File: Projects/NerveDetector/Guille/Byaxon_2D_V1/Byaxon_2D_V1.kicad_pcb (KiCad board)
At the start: 2 copper layers, 102 x 49 mm, 74 parts, among them U1 TL074

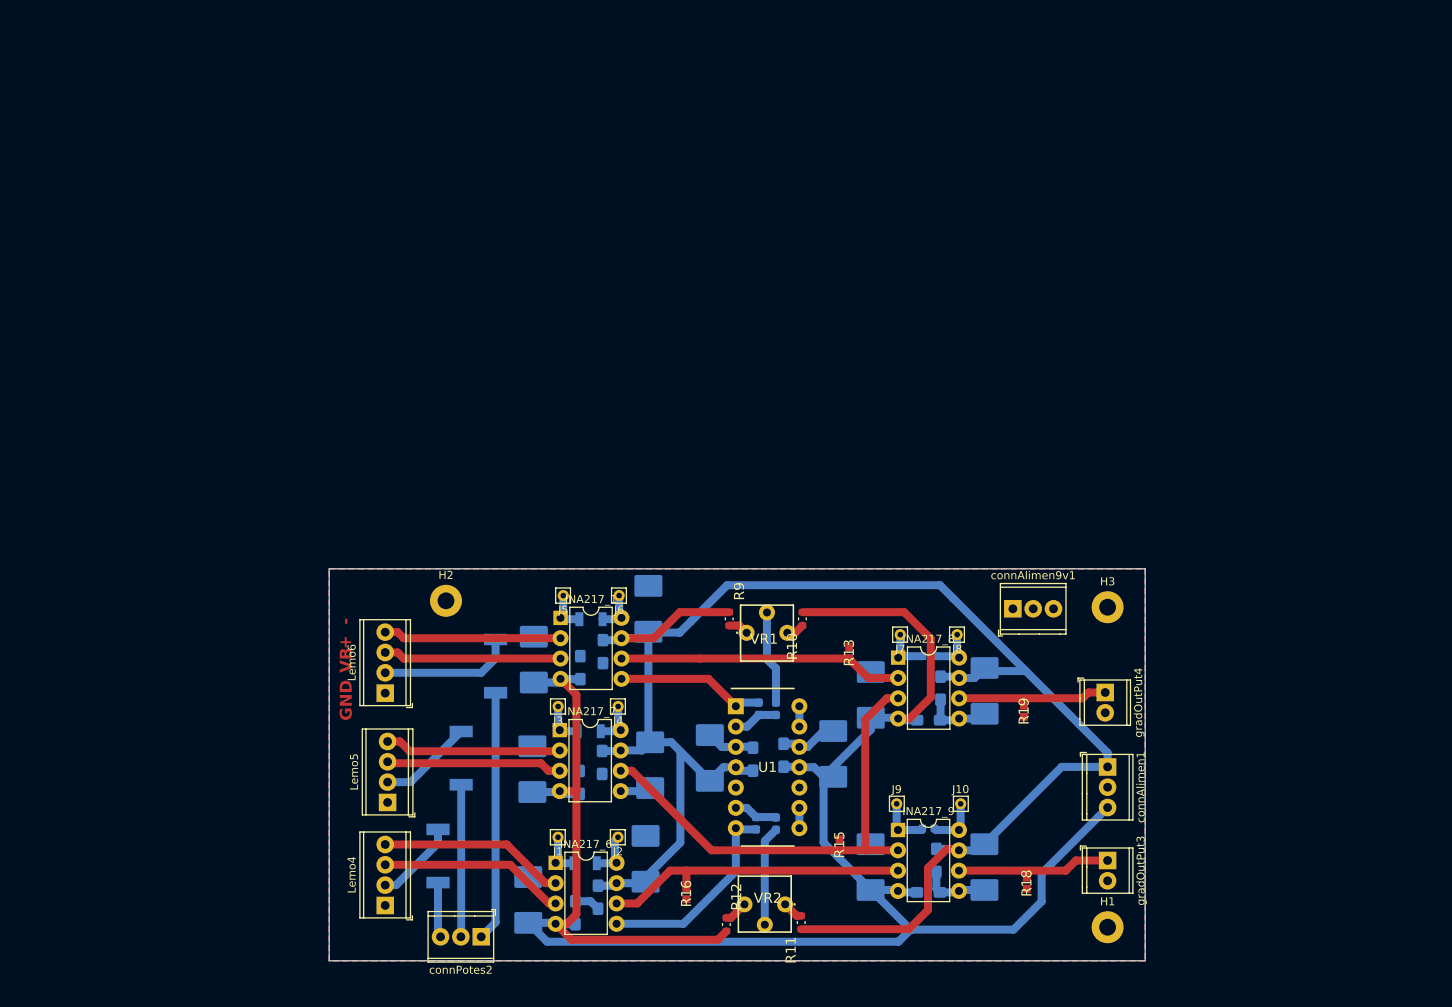
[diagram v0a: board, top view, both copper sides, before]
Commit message: Solved problem with footprint libraries missing
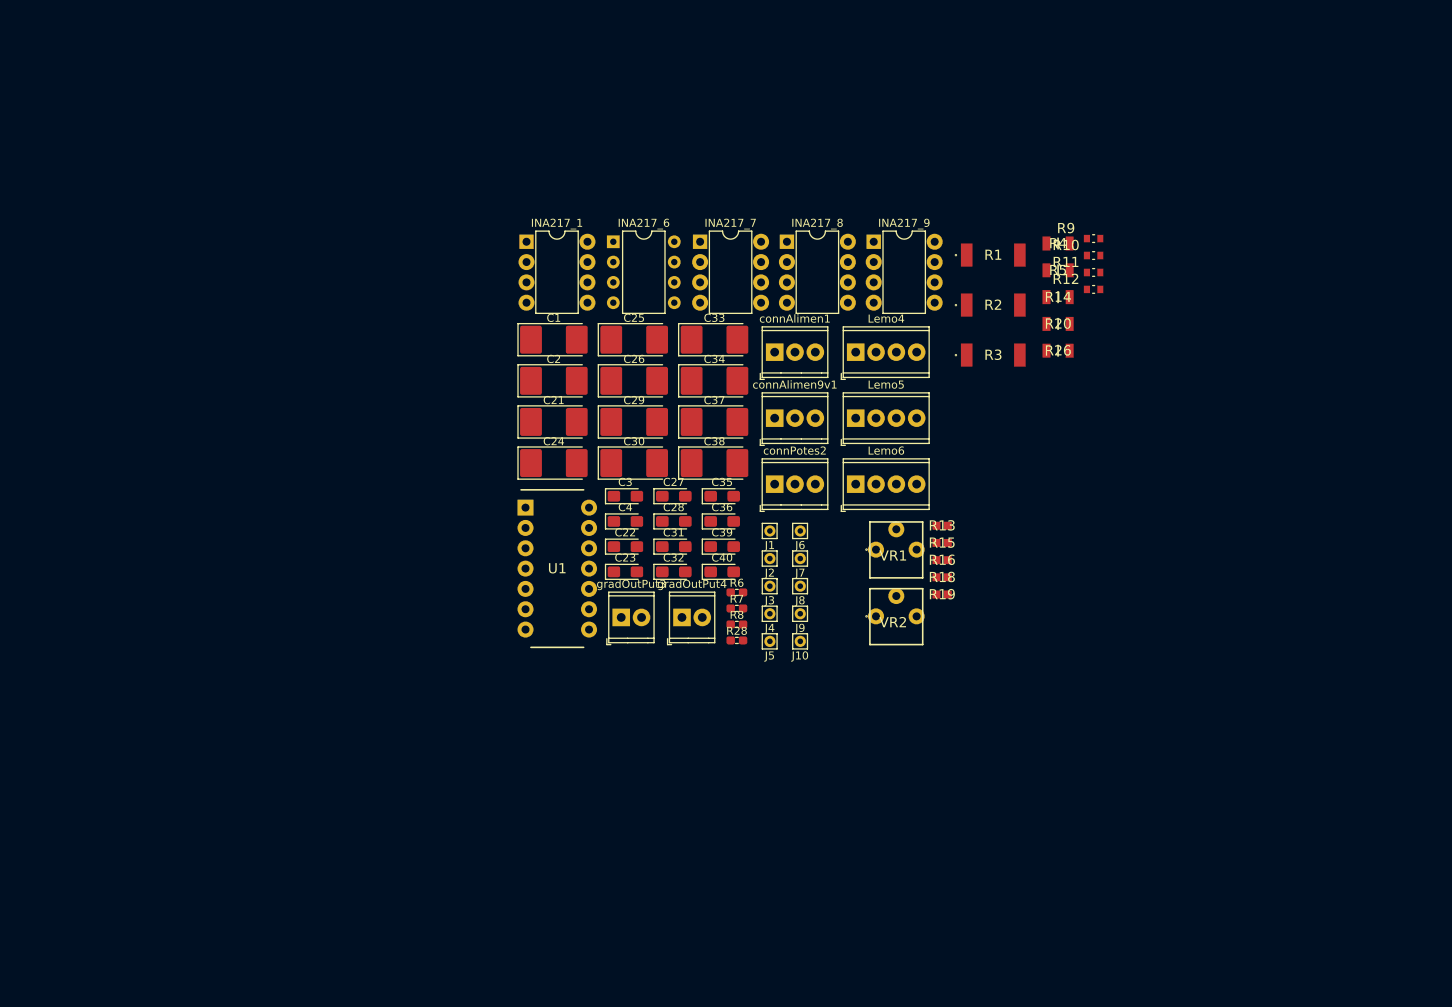
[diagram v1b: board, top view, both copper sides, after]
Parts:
- removed H1, H2, H3: MountingHole_Pad, Library_Acid_etch_limitations:MountingHole_2.1mm_Acid_Etch_Limitations
- C1, C2, C21, C22, C23, C24, C25, C26, C27, C28, C29, C3, C30, C31, C32, C33, C34, C35, C36, C37, C38, C39, C4, C40, R28, R6, R7, R8: moved to F.Cu
- R1, R2, R3: footprint SamacSys_Parts:ERJ1T__2512_ -> Samac_sys:ERJ1T__2512_; moved to F.Cu
- R10, R11, R12, R9: footprint SamacSys_Parts:RESC1608X60N -> Samac_sys:RESC1608X60N
- R14, R20: footprint SamacSys_Parts:RESC1608X55N -> Samac_sys:RESC3016X65N; moved to F.Cu
- R26, R4, R5: footprint SamacSys_Parts:RESC3016X65N -> Samac_sys:RESC3016X65N; moved to F.Cu
- moved R2 97.8 mm to (153.0, 73.0), turned to 0 degrees
- moved R5 94.8 mm to (161.1, 68.7)
- moved R12 91.7 mm to (165.6, 71.1), turned to 0 degrees
- moved R1 91.5 mm to (153.0, 66.8), turned to 0 degrees
- moved Lemo4 90.8 mm to (135.8, 78.9), turned to 0 degrees
- moved R11 89.1 mm to (165.6, 69.0), turned to 0 degrees
- moved R4 84.6 mm to (161.1, 65.3)
- moved C25 79.1 mm to (108.1, 77.4), turned to 0 degrees
- moved INA217_6 78.0 mm to (105.5, 65.1)
- moved Lemo5 75.7 mm to (135.8, 87.2), turned to 0 degrees
- moved INA217_9 73.6 mm to (138.1, 65.1)
- moved R3 73.4 mm to (153.0, 79.3), turned to 0 degrees
- moved R14 68.4 mm to (161.1, 72.0)
- moved gradOutPut3 68.0 mm to (106.5, 112.1), turned to 0 degrees
- moved connPotes2 67.4 mm to (125.7, 95.4), turned to 0 degrees
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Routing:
- net -13: track 239.3 -> 0.00 mm
- net +13: track 215.2 -> 0.00 mm
- net Net-(INA217_8-+): track 60.6 -> 0.00 mm
- net Net-(INA217_9-+): track 38.9 -> 0.00 mm
- net Earth: track 36.4 -> 0.00 mm
- net Net-(INA217_8--): track 35.6 -> 0.00 mm
- net Net-(connPotes2-Pin_1): track 31.3 -> 0.00 mm
- net Net-(INA217_6-Ref): track 25.6 -> 0.00 mm
- net Net-(INA217_6-+): track 23.3 -> 0.00 mm
- net Net-(INA217_6--): track 23.3 -> 0.00 mm
- net Net-(INA217_1-+): track 22.2 -> 0.00 mm
- net Net-(INA217_1--): track 22.2 -> 0.00 mm
- net Net-(INA217_7-+): track 22.0 -> 0.00 mm
- net Net-(INA217_7--): track 21.7 -> 0.00 mm
- net Net-(gradOutPut3-Pin_1): track 19.1 -> 0.00 mm
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- removed copper zone on B.Cu, net Earth
- removed copper zone on F.Cu, net Earth
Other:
- board outline removed
- board text removed: "+"
- board text removed: "-"
- board text removed: "GND"
- board text removed: "VB"

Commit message: Layed out bigger edge cut, added jumper to Voss
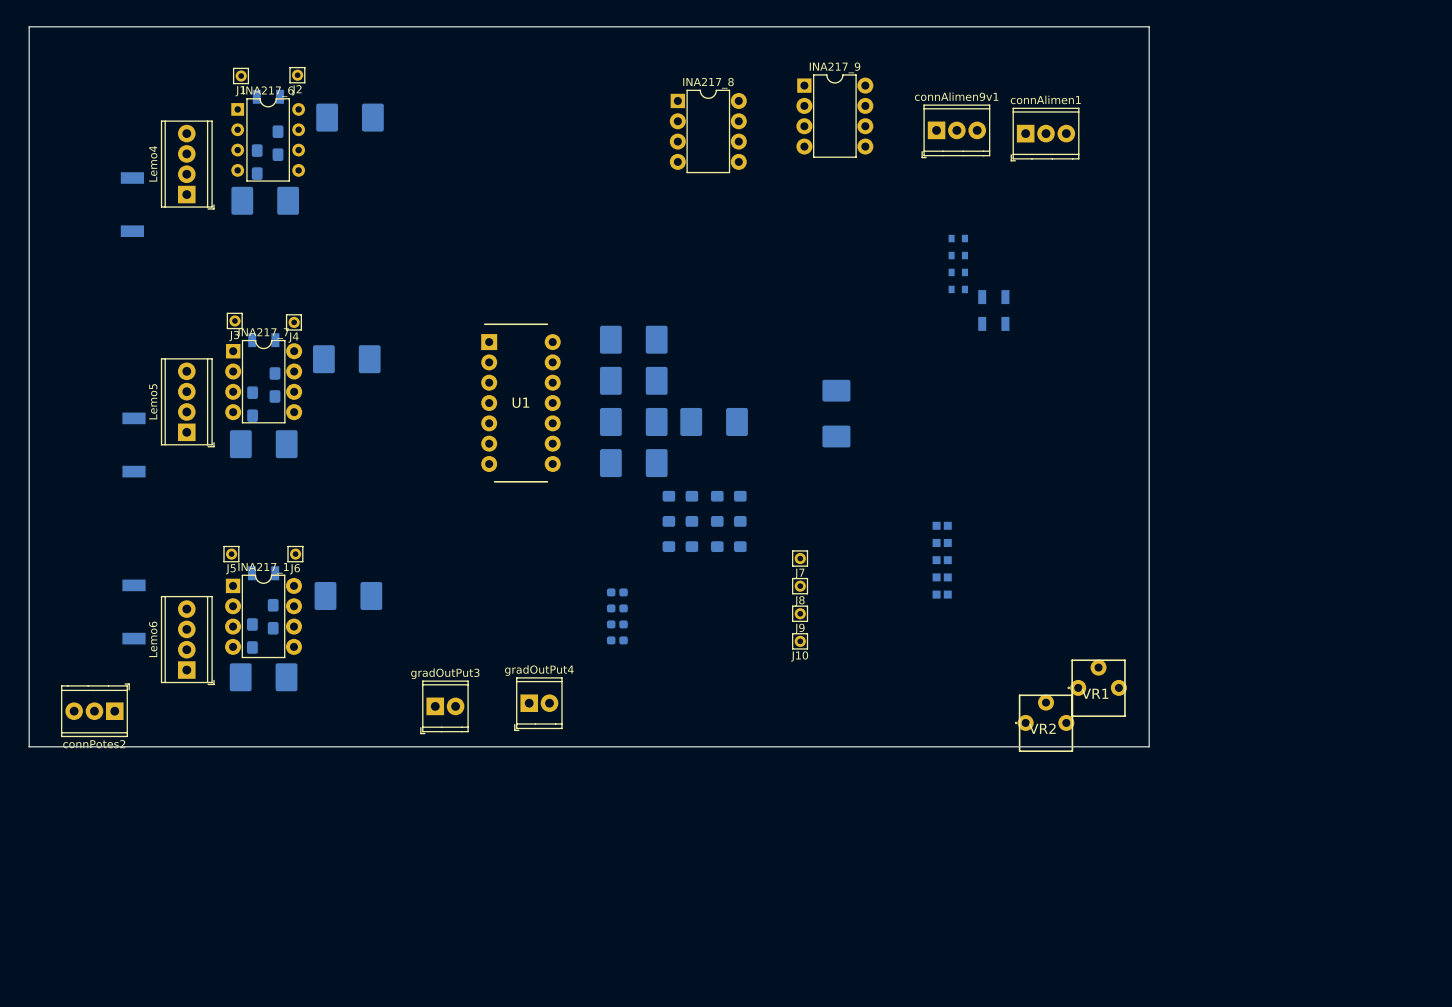
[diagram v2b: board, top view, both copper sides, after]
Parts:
- C1, C2, C21, C22, C23, C24, C25, C26, C27, C28, C29, C3, C30, C31, C32, C33, C34, C35, C36, C37, C38, C39, C4, C40, R1, R10, R11, R12, R13, R14, R15, R16, R18, R19, R2, R20, R26, R28, R3, R4, R5, R6, R7, R8, R9: moved to B.Cu
- moved R3 112.1 mm to (45.6, 111.4), turned to 90 degrees
- moved R1 110.0 mm to (45.6, 90.5), turned to -90 degrees
- moved R2 108.3 mm to (45.4, 60.5), turned to -90 degrees
- moved R26 103.1 mm to (61.8, 106.6)
- moved R5 101.1 mm to (62.4, 47.0), turned to 180 degrees
- moved R4 100.0 mm to (61.8, 77.4)
- moved connPotes2 87.2 mm to (43.2, 123.8), turned to 180 degrees
- moved J1 87.2 mm to (59.0, 44.4)
- moved Lemo6 86.8 mm to (52.2, 118.7), turned to 90 degrees
- moved Lemo4 85.9 mm to (52.2, 59.2), turned to 90 degrees
- moved J2 84.5 mm to (66.0, 44.3)
- moved Lemo5 83.6 mm to (52.2, 88.9), turned to 90 degrees
- moved J3 74.6 mm to (58.2, 75.0)
- moved C36 73.5 mm to (61.0, 55.2), turned to 90 degrees
- moved C35 70.9 mm to (63.6, 52.8), turned to 90 degrees
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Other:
- board outline added: 140 x 90 mm

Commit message: Changed jumpers + some layout
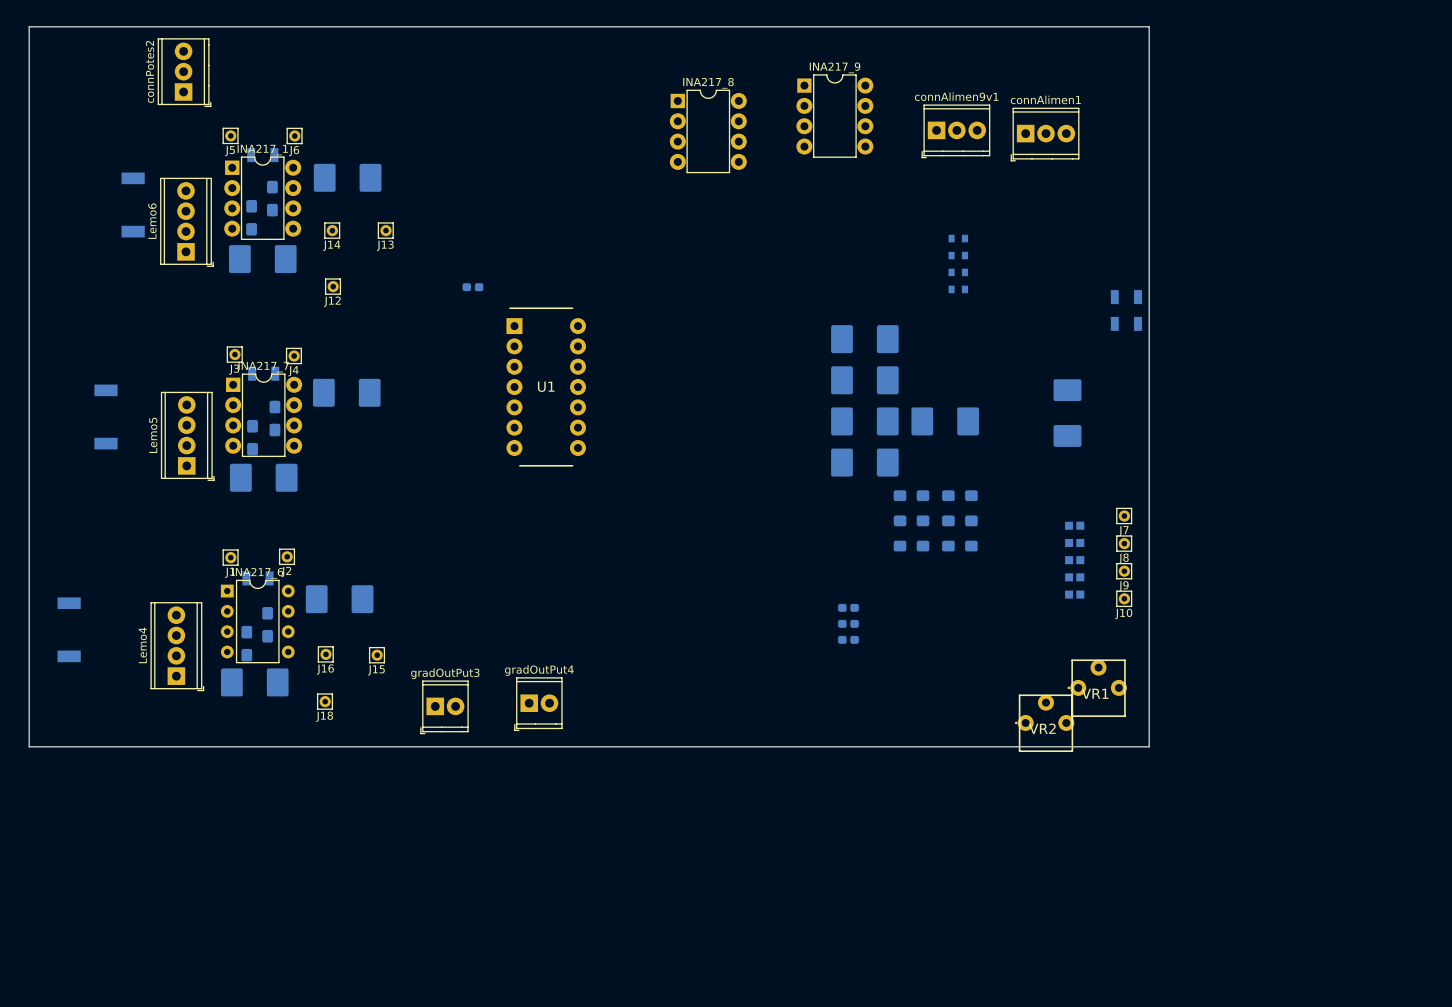
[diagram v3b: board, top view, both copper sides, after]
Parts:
- added J12: ~, Connector_Pin:Pin_D0.7mm_L6.5mm_W1.8mm_FlatFork, F.Cu at (70.5, 70.7)
- added J13: ~, Connector_Pin:Pin_D0.7mm_L6.5mm_W1.8mm_FlatFork, F.Cu at (77.1, 63.7)
- added J14: ~, Connector_Pin:Pin_D0.7mm_L6.5mm_W1.8mm_FlatFork, F.Cu at (70.4, 63.7)
- added J15: ~, Connector_Pin:Pin_D0.7mm_L6.5mm_W1.8mm_FlatFork, F.Cu at (76.0, 116.8)
- added J16: ~, Connector_Pin:Pin_D0.7mm_L6.5mm_W1.8mm_FlatFork, F.Cu at (69.6, 116.7)
- added J18: ~, Connector_Pin:Pin_D0.7mm_L6.5mm_W1.8mm_FlatFork, F.Cu at (69.5, 122.6)
- moved connPotes2 77.9 mm to (51.8, 46.4), turned to 90 degrees
- moved C2 60.2 mm to (60.7, 120.2)
- moved C35 60.2 mm to (62.3, 113.0)
- moved INA217_6 60.2 mm to (57.3, 108.8)
- moved J2 60.2 mm to (64.8, 104.5)
- moved Lemo4 60.2 mm to (50.9, 119.4)
- moved R5 60.2 mm to (61.1, 107.2)
- moved C33 60.2 mm to (71.3, 109.8)
- moved C36 60.2 mm to (59.7, 115.4)
- moved J1 60.2 mm to (57.7, 104.6)
- moved R2 53.7 mm to (37.5, 113.6), turned to 90 degrees
- moved C32 52.3 mm to (60.3, 62.1)
- moved C37 52.3 mm to (72.3, 57.1)
- moved C38 52.3 mm to (61.7, 67.3)
- moved Lemo6 52.3 mm to (52.1, 66.4)
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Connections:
- R6 pad 2: Net-(INA217_1-Ref) -> Net-(J13-Pin_1)
- R7 pad 2: Net-(INA217_6-Ref) -> Net-(J15-Pin_1)
- U1 pad 1: Net-(INA217_1-Ref) -> Net-(J13-Pin_1)
- U1 pad 7: Net-(INA217_6-Ref) -> Net-(J15-Pin_1)

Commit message: Final commit of the day - Some layout
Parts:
- moved R16 92.3 mm to (71.8, 92.3), turned to -90 degrees
- moved VR1 86.9 mm to (96.4, 72.5)
- moved C26 83.4 mm to (62.6, 120.2), turned to 0 degrees
- moved R13 80.9 mm to (95.2, 56.8), turned to 90 degrees
- moved gradOutPut4 78.0 mm to (144.5, 62.5), turned to 90 degrees
- moved C1 73.6 mm to (88.7, 87.2)
- moved J7 70.3 mm to (116.5, 53.1)
- moved R15 69.6 mm to (95.4, 118.4), turned to -90 degrees
- moved VR2 69.0 mm to (96.7, 100.4), turned to 180 degrees
- moved J8 67.1 mm to (124.4, 53.1)
- moved INA217_9 64.9 mm to (116.5, 109.2)
- moved R12 62.1 mm to (93.4, 99.3)
- moved gradOutPut3 62.0 mm to (144.5, 113.6), turned to 90 degrees
- moved R14 60.8 mm to (120.2, 107.4), turned to 0 degrees
- moved C2 57.1 mm to (104.4, 83.3), turned to 90 degrees
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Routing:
- net -13: track 0.00 -> 35.6 mm
- net +13: track 0.00 -> 34.2 mm
- net Earth: track 0.00 -> 33.1 mm
- net Net-(J8-Pin_1): track 0.00 -> 7.43 mm
- net Net-(J1-Pin_1): track 0.00 -> 7.41 mm
- net Net-(J7-Pin_1): track 0.00 -> 7.38 mm
- net Net-(J2-Pin_1): track 0.00 -> 7.32 mm
- net Net-(J5-Pin_1): track 0.00 -> 7.08 mm
- net Net-(J10-Pin_1): track 0.00 -> 7.06 mm
- net Net-(J6-Pin_1): track 0.00 -> 7.05 mm
- net Net-(J9-Pin_1): track 0.00 -> 6.89 mm
- net Net-(J3-Pin_1): track 0.00 -> 6.81 mm
- net Net-(J4-Pin_1): track 0.00 -> 6.52 mm
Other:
- board size 140 x 90 mm -> 120.3 x 90 mm

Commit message: Finished layout
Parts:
- moved R15 31.5 mm to (76.8, 93.0), turned to 0 degrees
- moved R16 27.9 mm to (86.8, 115.8)
- moved R11 10.2 mm to (93.0, 106.4), turned to 0 degrees
- moved R12 9.70 mm to (100.0, 106.4), turned to 0 degrees
- moved R10 7.61 mm to (100.2, 65.8)
- moved R9 7.61 mm to (92.9, 65.8)
- moved VR2 4.79 mm to (96.7, 105.2), turned to 0 degrees
- moved connAlimen1 3.78 mm to (144.2, 84.6), turned to -90 degrees
- moved gradOutPut3 3.75 mm to (144.5, 117.4)
- moved R13 3.30 mm to (95.2, 60.1)
- moved C2 1.70 mm to (106.1, 83.2)
- moved VR1 1.60 mm to (96.4, 74.1)
- moved gradOutPut4 1.55 mm to (144.9, 64.0)
- moved R19 1.35 mm to (132.4, 64.8)
- moved Lemo4 0.40 mm to (50.9, 119.0)
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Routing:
- net +13: track 34.2 -> 394.4 mm, vias 0 -> 8
- net -13: track 35.6 -> 369.2 mm, vias 0 -> 8
- net Net-(INA217_8-+): track 0.00 -> 117.1 mm
- net Net-(connPotes2-Pin_3): track 0.00 -> 74.4 mm
- net Net-(INA217_9-+): track 0.00 -> 52.4 mm
- net Net-(INA217_8--): track 0.00 -> 51.6 mm
- net Net-(connPotes2-Pin_2): track 0.00 -> 44.6 mm
- net Net-(J15-Pin_1): track 0.00 -> 38.6 mm, vias 0 -> 1
- net Earth: track 33.1 -> 58.1 mm
- net Net-(J13-Pin_1): track 0.00 -> 24.4 mm
- net Net-(gradOutPut3-Pin_1): track 0.00 -> 21.7 mm
- net Net-(gradOutPut4-Pin_1): track 0.00 -> 21.4 mm
- net Net-(connPotes2-Pin_1): track 0.00 -> 12.8 mm
- net Net-(Lemo4-Pin_2): track 0.00 -> 11.1 mm
- net Net-(R28-Pad1): track 0.00 -> 11.1 mm
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- added copper zone on B.Cu, net Earth
- added copper zone on F.Cu, net Earth
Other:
- board text added: "+13"
- board text added: "-13"
- board text added: "CH1"
- board text added: "CH2"
- board text added: "GND"
- board text added: "POT"
- board text added: "REF"
- board text added: "TIE GNDs"
- board text added: "VOSS"
